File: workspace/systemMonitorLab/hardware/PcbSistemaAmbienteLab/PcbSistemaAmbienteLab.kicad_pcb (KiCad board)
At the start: 2 copper layers, 7 parts, among them J1 Conn_01x01_Male, J2 Conn_01x01_Male, U1 DHT22, U2 AHT10, U3 Bmp280Module, U4 NodeMcuEsp8266

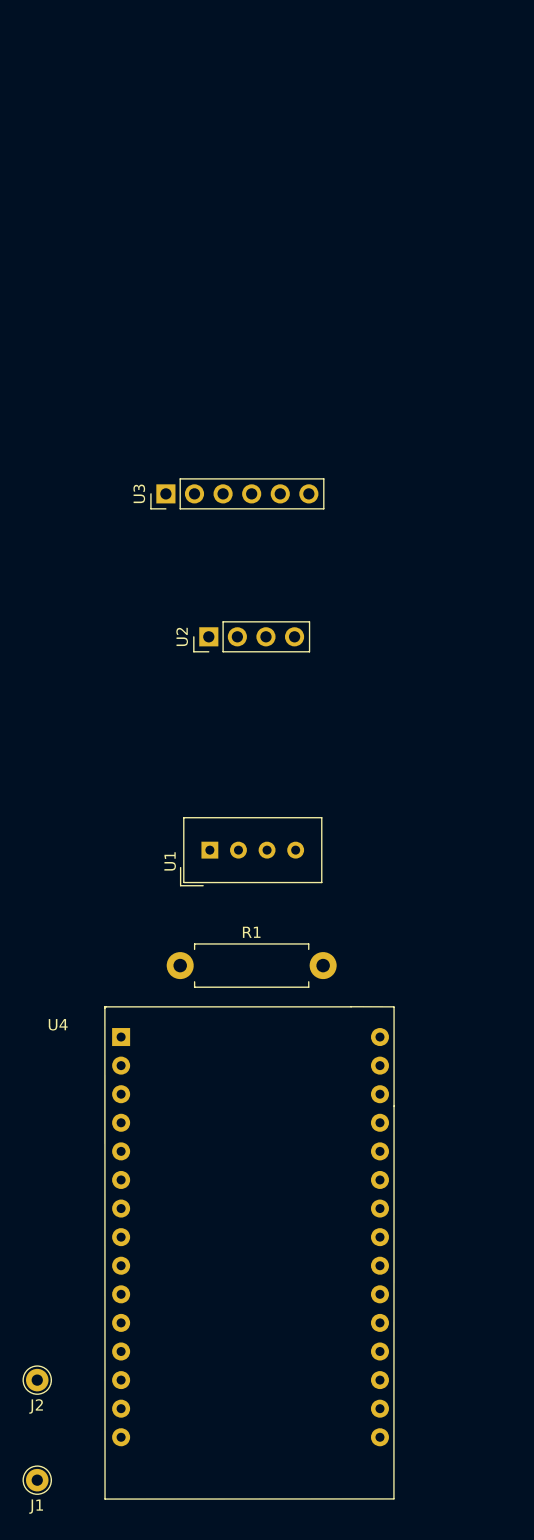
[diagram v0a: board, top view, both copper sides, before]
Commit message: Esquematico y PCB para sistema de monitoreo v1.1
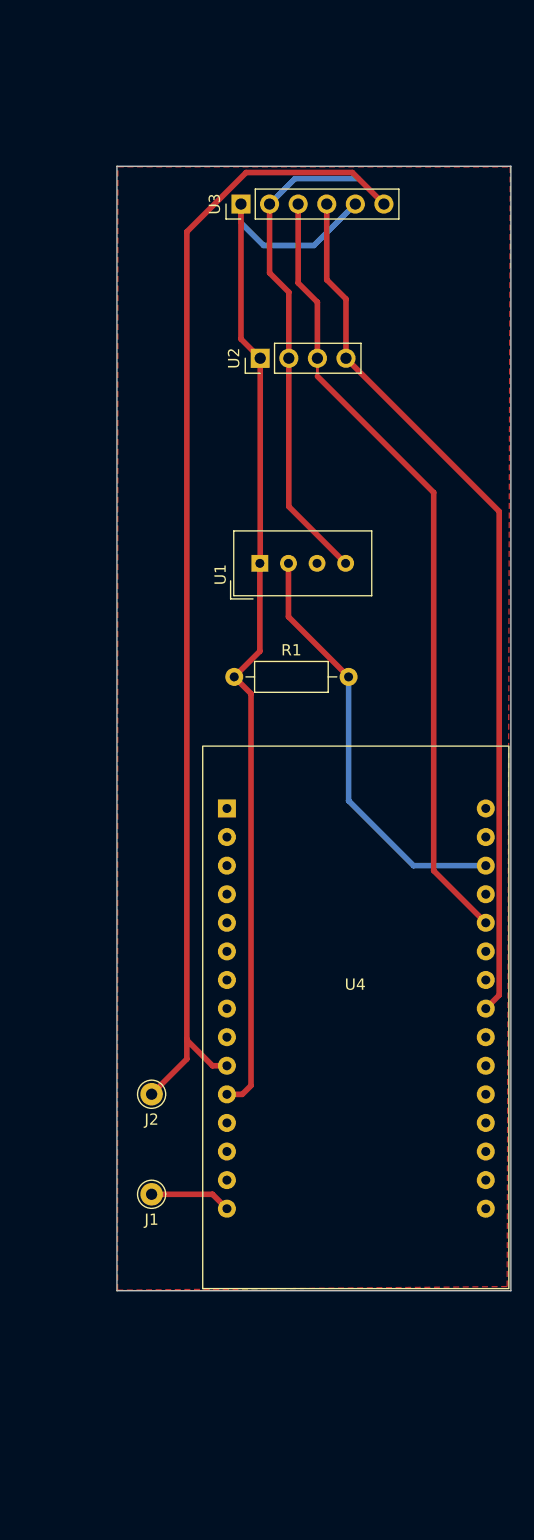
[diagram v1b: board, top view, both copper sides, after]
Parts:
- R1: footprint Resistor_THT:R_Axial_DIN0411_L9.9mm_D3.6mm_P12.70mm_Horizontal -> Resistor_THT:R_Axial_DIN0207_L6.3mm_D2.5mm_P10.16mm_Horizontal
- U4: footprint NodeMCU_Module:ES8266 -> NodeMCU_Module:ESP8266
- moved J1 27.4 mm to (133.3, 124.5)
- moved J2 27.4 mm to (133.3, 115.6)
- moved U3 26.6 mm to (141.3, 36.5)
- moved R1 26.1 mm to (140.7, 78.5)
- moved U1 25.9 mm to (143.0, 68.4)
- moved U2 25.2 mm to (143.0, 50.2)
- moved U4 22.4 mm to (151.6, 111.8)
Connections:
- R1 pad 1: +5V -> 3V3
- U4 pad 10: unconnected-(U4-Pad10) -> GND
- U4 pad 14: GND -> unconnected-(U4-Pad14)
- U4 pad 16: GND -> unconnected-(U4-Pad16)
- U4 pad 17: 3V3 -> unconnected-(U4-Pad17)
- U4 pad 24: GND -> unconnected-(U4-Pad24)
- U4 pad 25: 3V3 -> unconnected-(U4-Pad25)
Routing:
- net GND: track 0.00 -> 150.1 mm
- net 3V3: track 0.00 -> 97.3 mm
- net Net-(U2-Pad4): track 0.00 -> 78.3 mm
- net Net-(U2-Pad3): track 0.00 -> 70.8 mm
- net Net-(R1-Pad2): track 0.00 -> 37.9 mm
- net +5V: track 0.00 -> 7.22 mm
- added copper zone on F.Cu, net GND
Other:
- board outline added: 35 x 99.9 mm

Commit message: subo v1.2 del PCB del sistema de monitoreo ambiente, esta versión se utilizara para calibrar el sensor AHT10 vs DHT22
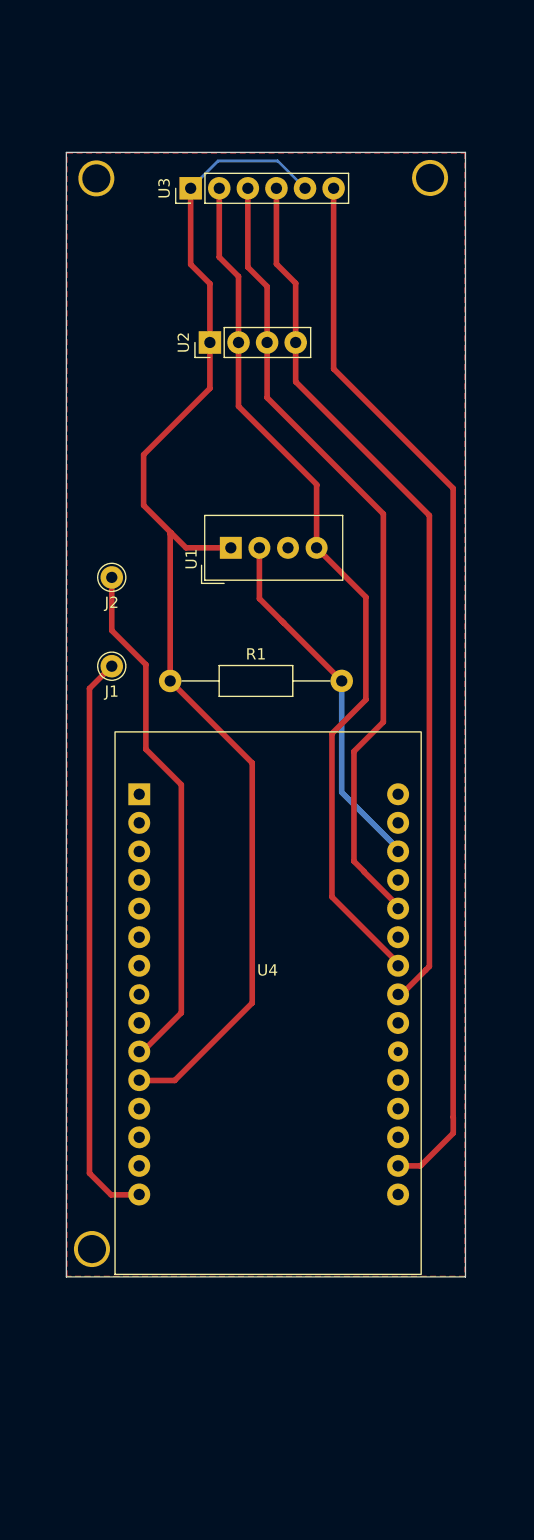
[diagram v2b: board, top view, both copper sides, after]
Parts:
- added ?: , clipboard:7c473ef6-f9f9-49c1-b1c9-f209bb782990, F.Cu at (128.1, 129.3)
- added ?: , clipboard:7c473ef6-f9f9-49c1-b1c9-f209bb782990, F.Cu at (128.4, 34.2)
- added ?: , clipboard:7c473ef6-f9f9-49c1-b1c9-f209bb782990, F.Cu at (158.1, 34.2)
- R1: footprint Resistor_THT:R_Axial_DIN0207_L6.3mm_D2.5mm_P10.16mm_Horizontal -> Resistor_THT:R_Axial_DIN0207_L6.3mm_D2.5mm_P15.24mm_Horizontal
- moved J1 47.1 mm to (129.8, 77.5)
- moved J2 46.1 mm to (129.8, 69.7)
- moved U4 7.89 mm to (143.8, 110.5)
- moved R1 5.70 mm to (135.0, 78.8)
- moved U2 4.68 mm to (138.5, 48.8)
- moved U3 4.68 mm to (136.8, 35.1)
- moved U1 2.93 mm to (140.4, 67.0)
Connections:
- U4 pad 17: unconnected-(U4-Pad17) -> GND
- U4 pad 24: unconnected-(U4-Pad24) -> GND
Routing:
- net GND: track 150.1 -> 218.9 mm
- net +5V: track 7.22 -> 51.4 mm
- net 3V3: track 97.3 -> 110.2 mm
- net Net-(R1-Pad2): track 37.9 -> 32.6 mm
- net Net-(U2-Pad3): track 70.8 -> 71.8 mm
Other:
- board size 35 x 99.9 mm -> 35.5 x 99.9 mm

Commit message: Dejo transmitiendo cada 1 minuto
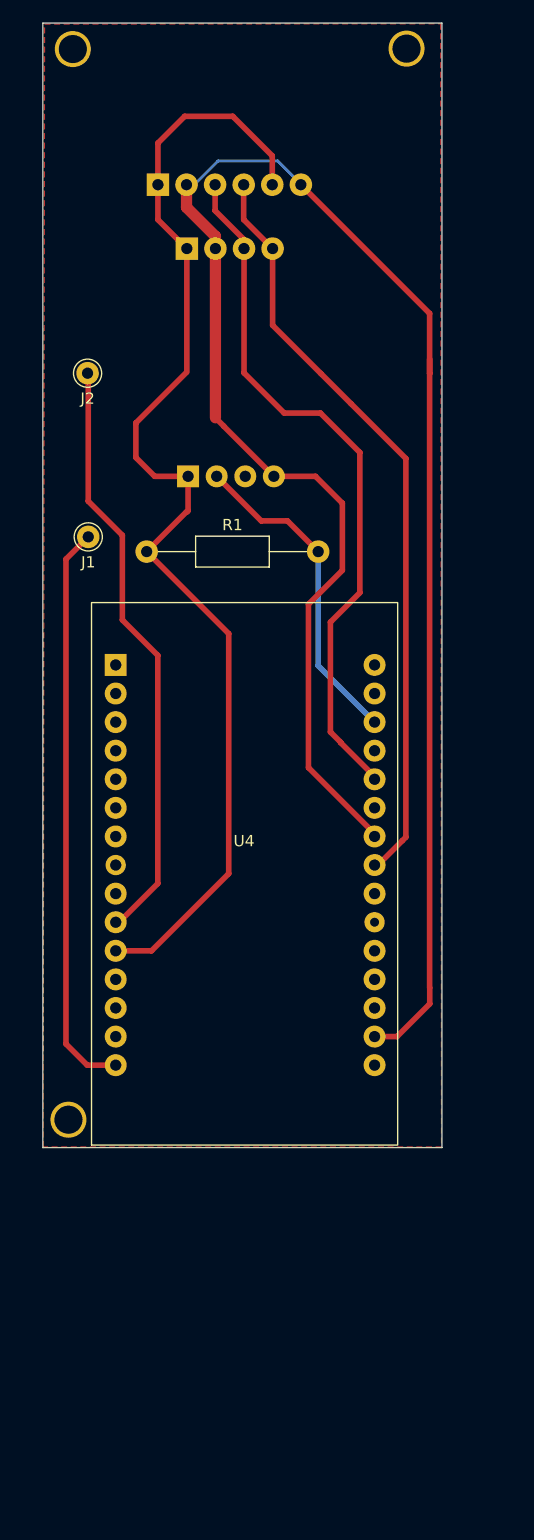
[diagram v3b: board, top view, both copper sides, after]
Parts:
- U1, U2, U3: moved to B.Cu
- moved J2 18.3 mm to (127.7, 51.5)
- moved J1 11.7 mm to (127.7, 66.0)
- moved U4 11.7 mm to (141.8, 99.0)
- moved ? 11.7 mm to (126.3, 22.7)
- moved ? 11.7 mm to (126.0, 117.8)
- moved ? 11.7 mm to (156.0, 22.7)
- moved R1 11.7 mm to (132.9, 67.4)
- moved U2 8.59 mm to (136.5, 40.4), turned to -90 degrees
- moved U1 7.40 mm to (136.6, 60.7), turned to -90 degrees
- moved U3 2.93 mm to (133.9, 34.8), turned to -90 degrees
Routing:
- net Net-(U2-Pad4): track 78.3 -> 67.5 mm
- net Net-(U2-Pad3): track 71.8 -> 62.7 mm
- net 3V3: track 110.2 -> 104.3 mm
- net Net-(R1-Pad2): track 32.6 -> 29.0 mm
- net GND: track 218.9 -> 219.7 mm
